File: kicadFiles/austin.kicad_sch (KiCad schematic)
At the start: 558 parts, among them J1 EXTRA PINS, J2 ARM SWD, J3 TYPE-C-31-M-12, Q1 DTC123JKAT146, Q2 AO3401A, Q3 DTC123JKAT146, SW1 K2-1187SQ-A4SW-06, SW10 MXSwitch, SW100 MXSwitch, SW101 MXSwitch, SW102 MXSwitch, SW103 MXSwitch, SW104 MXSwitch, SW105 MXSwitch, SW106 MXSwitch, SW107 MXSwitch, SW108 MXSwitch, SW109 MXSwitch, SW11 MXSwitch, SW110 MXSwitch, SW111 MXSwitch, SW112 MXSwitch, SW113 MXSwitch, SW114 MXSwitch, SW115 MXSwitch, SW116 MXSwitch, SW12 MXSwitch, SW13 MXSwitch, SW14 MXSwitch, SW15 MXSwitch, SW16 MXSwitch, SW17 MXSwitch, SW18 MXSwitch, SW19 MXSwitch, SW2 PCM12SMTR, SW20 MXSwitch, SW21 MXSwitch, SW22 MXSwitch, SW23 MXSwitch, SW24 MXSwitch, SW25 MXSwitch, SW26 MXSwitch, SW27 MXSwitch, SW28 MXSwitch, SW29 MXSwitch, SW3 MXSwitch, SW30 MXSwitch, SW31 MXSwitch, SW32 MXSwitch, SW33 MXSwitch, SW34 MXSwitch, SW35 MXSwitch, SW36 MXSwitch, SW37 MXSwitch, SW38 MXSwitch, SW39 MXSwitch, SW4 MXSwitch, SW40 MXSwitch, SW41 MXSwitch, SW42 MXSwitch, SW43 MXSwitch, SW44 MXSwitch, SW45 MXSwitch, SW46 MXSwitch, SW47 MXSwitch, SW48 MXSwitch, SW49 MXSwitch, SW5 MXSwitch, SW50 MXSwitch, SW51 MXSwitch, SW52 MXSwitch, SW53 MXSwitch, SW54 MXSwitch, SW55 MXSwitch, SW56 MXSwitch, SW57 MXSwitch, SW58 MXSwitch, SW59 MXSwitch, SW6 MXSwitch, SW60 MXSwitch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

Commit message: Add further component metadata
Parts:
- C12, C13, C9: Package (none) -> C0402
- LED1, LED2, LED67: now left out of the parts list
- R10, R9: Package (none) -> R0805
- R8: value 100 -> 100R; Package (none) -> R0805
- SW2: LCSC Part Number (none) -> C221841; Manufacturer Part Number (none) -> PCM12SMTR
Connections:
- net 5V: no longer D2.1 (K)
- net VBUS: now also D2.1 (K)
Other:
- note removed: "B"
- note removed: "C"
- note removed: "E"
- note removed: "F"
- note removed: "I"
- note removed: "M"
- note removed: "N"
- note removed: "O"
- note removed: "P"
- note removed: "Q"
- note removed: "R"
- note removed: "T"
- note removed: "Tab"
- note removed: "U"
- note removed: "V"
- note removed: "W"
- note removed: "X"
- note removed: "Y"
- note removed: "Z"
- note removed: "[{"
- note removed: "]}"
- moved on the sheet: C14, C15, C16, C17, C18, C19, C20, C21, C22, C23, C24, C25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

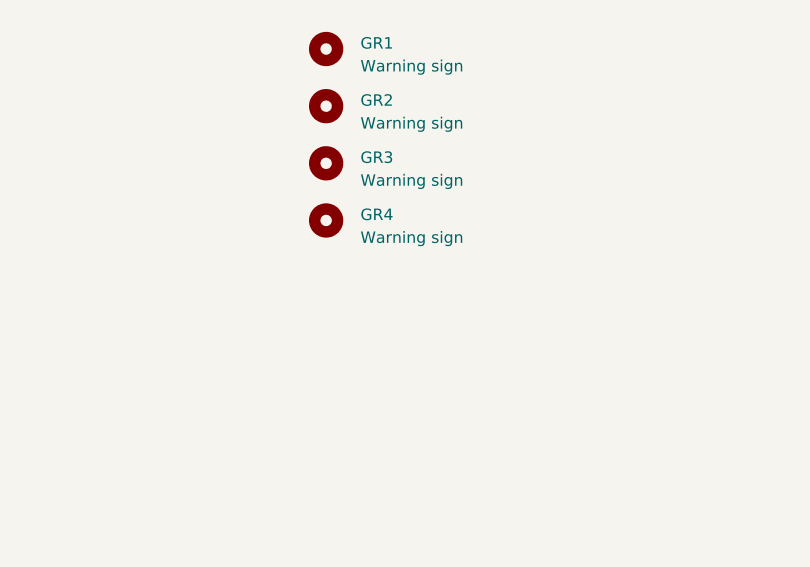
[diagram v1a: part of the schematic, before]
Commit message: Add warning sign to numpad
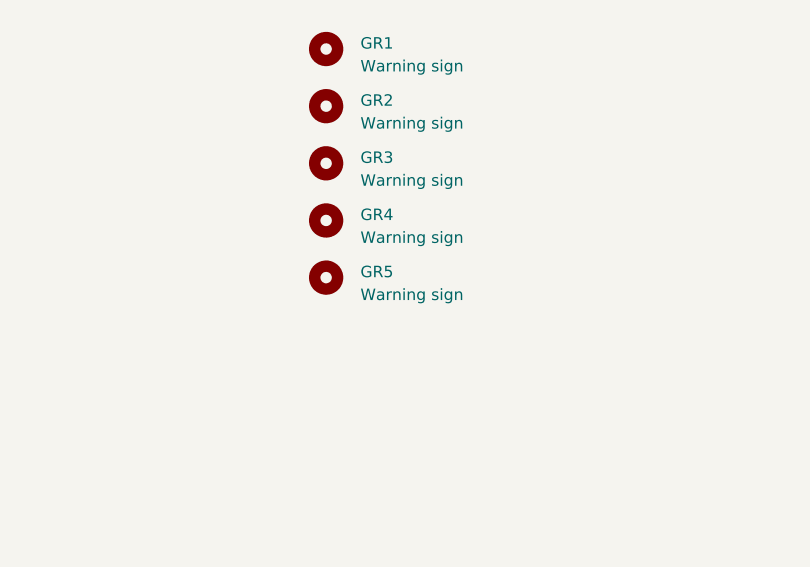
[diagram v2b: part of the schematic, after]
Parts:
- added GR5: Warning sign, acheron_Graphics:warning_sign_3.6x3.2mm, symbol Mechanical:MountingHole
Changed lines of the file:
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@@
   (title_block
     (title "AustinPCB")
-    (date "2021-03-21")
-    (rev "v2.1.2")
+    (date "2021-03-26")
+    (rev "v2.1.3")
     (company "Designed by Gondolindrim")
     (comment 1 "In partnership with driftingbunnies and PheonixStar")
@@
     )
   )
+  (symbol (lib_name "Mechanical:MountingHole_2") (lib_id "Mechanical:MountingHole") (at 520.7 57.15 0) (unit 1)
+    (in_bom no) (on_board yes)
+    (property "Reference" "GR5" (id 0) (at 524.51 56.5149 0)
+      (effects (font (size 1.27 1.27)) (justify left))
+    )
+    (property "Value" "Warning sign" (id 1) (at 524.51 59.0549 0)
+      (effects (font (size 1.27 1.27)) (justify left))
+    )
+    (property "Footprint" "acheron_Graphics:warning_sign_3.6x3.2mm" (id 2) (at 520.7 57.15 0)
+      (effects (font (size 1.27 1.27)) hide)
+    )
+    (property "Datasheet" "~" (id 3) (at 520.7 57.15 0)
+      (effects (font (size 1.27 1.27)) hide)
+    )
+  )
   (symbol (lib_id "Device:CP_Small") (at 370.205 48.895 0) (unit 1)
     (in_bom yes) (on_board yes)
@@
       (reference "GR4") (unit 1) (value "Warning sign") (footprint "acheron_Graphics:warning_sign_3.6x3.2mm")
     )
+    (path "/7fd7ad30-67a6-4394-a19a-b7b0f4d1595f"
+      (reference "GR5") (unit 1) (value "Warning sign") (footprint "acheron_Graphics:warning_sign_3.6x3.2mm")
+    )
     (path "/61a17a8a-02a8-413c-bfdf-6da380f643f3"
